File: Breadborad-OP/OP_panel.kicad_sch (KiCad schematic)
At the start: 30 parts, among them J1 Conn_01x04_Pin, J2 Conn_01x04_Pin, J4 Conn_01x04_Pin, U1 NE5532, U2 LM311

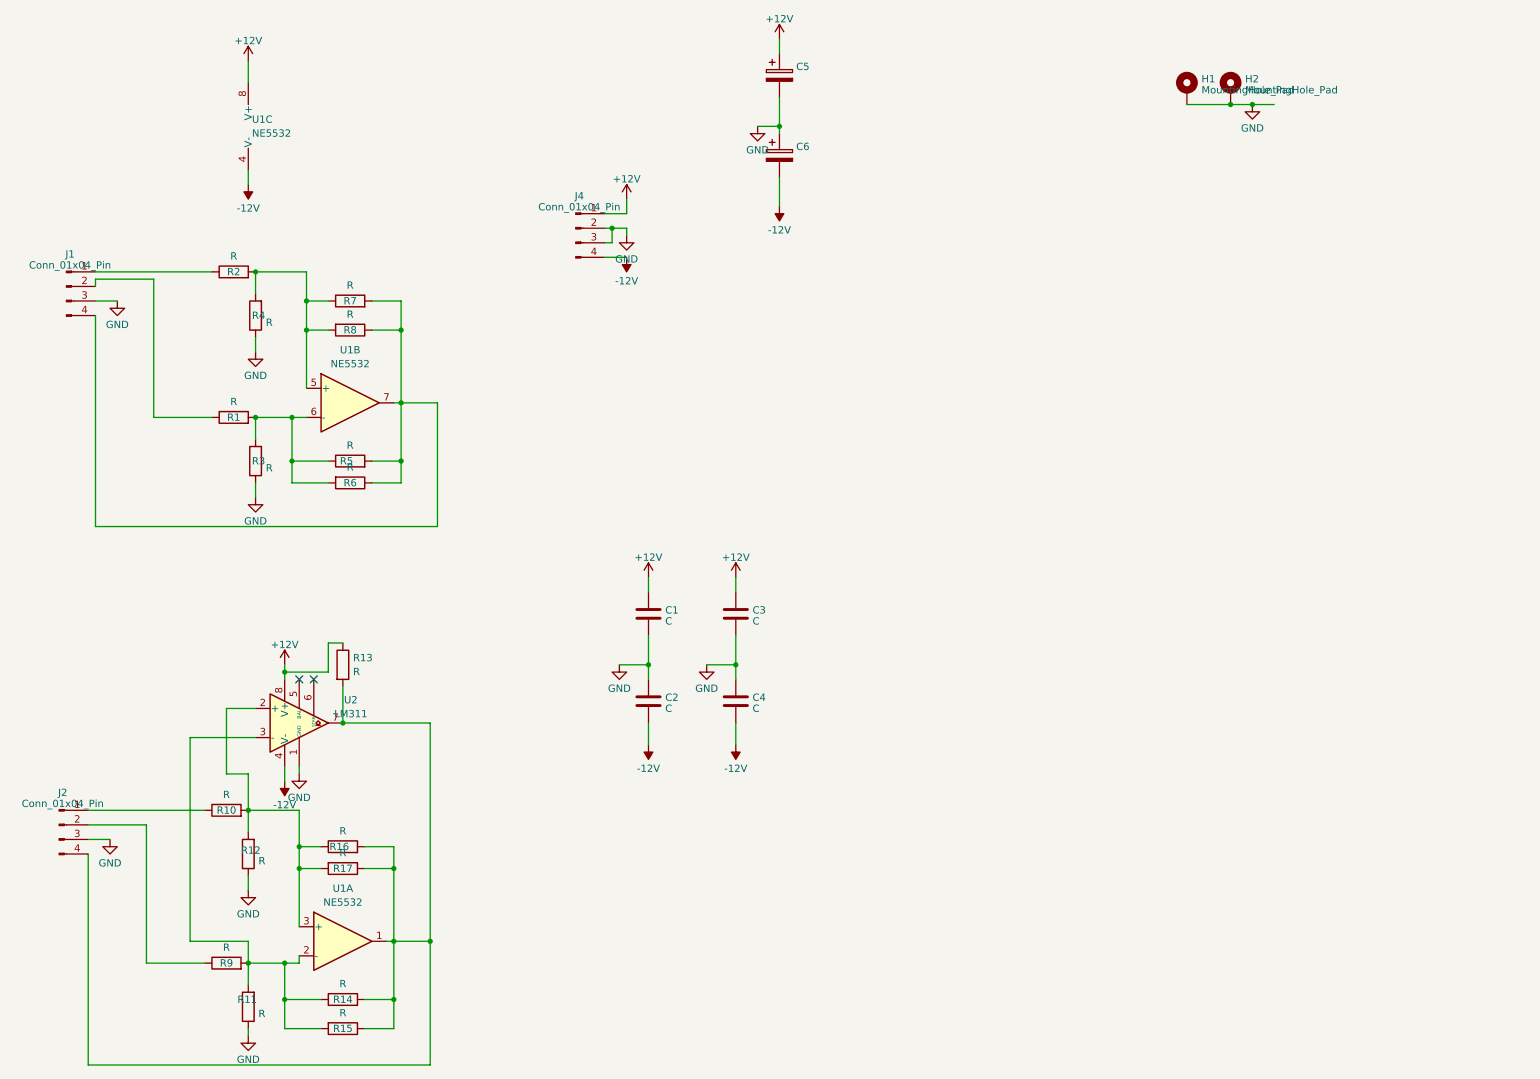
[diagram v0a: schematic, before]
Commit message: Anschlussleiste auf 2,56 mm Rastermaß geändert.
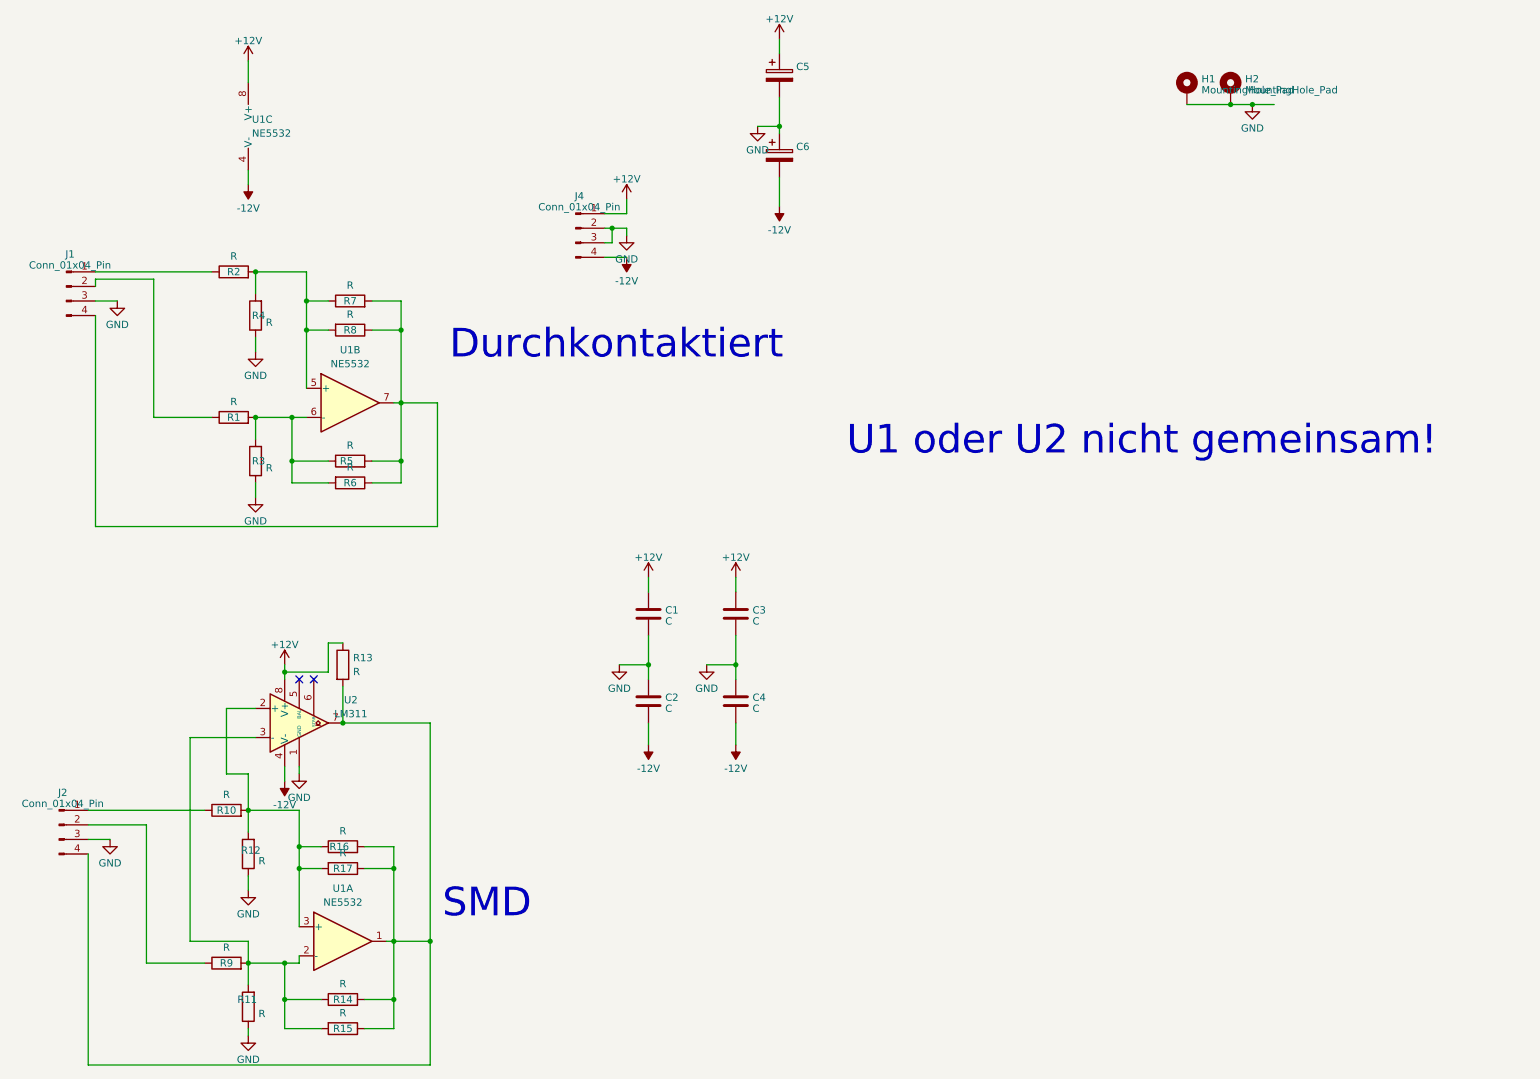
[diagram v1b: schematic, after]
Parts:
- J1, J2: footprint Connector_PinHeader_1.27mm:PinHeader_1x04_P1.27mm_Vertical -> Connector_PinHeader_2.54mm:PinHeader_1x04_P2.54mm_Vertical
- J4: footprint Connector_PinSocket_1.27mm:PinSocket_1x04_P1.27mm_Vertical -> Connector_PinSocket_2.54mm:PinSocket_1x04_P2.54mm_Vertical
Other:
- note added: "Durchkontaktiert"
- note added: "SMD"
- note added: "U1 oder U2 nicht gemeinsam!"
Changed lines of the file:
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@@
+		)
+	)
+	(text "U1 oder U2 nicht gemeinsam!"
+		(exclude_from_sim no)
+		(at 214.376 86.614 0)
+		(effects
+			(font
+				(size 5 5)
+			)
+		)
+	)
+	(text "Durchkontaktiert"
+		(exclude_from_sim no)
+		(at 122.682 69.85 0)
+		(effects
+			(font
+				(size 5 5)
+			)
+		)
+	)
+	(text "SMD"
+		(exclude_from_sim no)
+		(at 100.076 167.386 0)
+		(effects
+			(font
+				(size 5 5)
+			)
 		)
 	)
@@
 			)
 		)
-		(property "Footprint" "Connector_PinHeader_1.27mm:PinHeader_1x04_P1.27mm_Vertical"
+		(property "Footprint" "Connector_PinHeader_2.54mm:PinHeader_1x04_P2.54mm_Vertical"
 			(at 25.4 153.67 0)
 			(effects
@@
 			)
 		)
-		(property "Footprint" "Connector_PinHeader_1.27mm:PinHeader_1x04_P1.27mm_Vertical"
+		(property "Footprint" "Connector_PinHeader_2.54mm:PinHeader_1x04_P2.54mm_Vertical"
 			(at 26.67 59.69 0)
 			(effects
@@
 			)
 		)
-		(property "Footprint" "Connector_PinSocket_1.27mm:PinSocket_1x04_P1.27mm_Vertical"
+		(property "Footprint" "Connector_PinSocket_2.54mm:PinSocket_1x04_P2.54mm_Vertical"
 			(at 115.57 49.53 0)
 			(effects
